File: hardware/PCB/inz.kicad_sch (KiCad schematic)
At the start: 15 parts, among them J101 TP4056, J102 Battery, J103 STM32blackpill

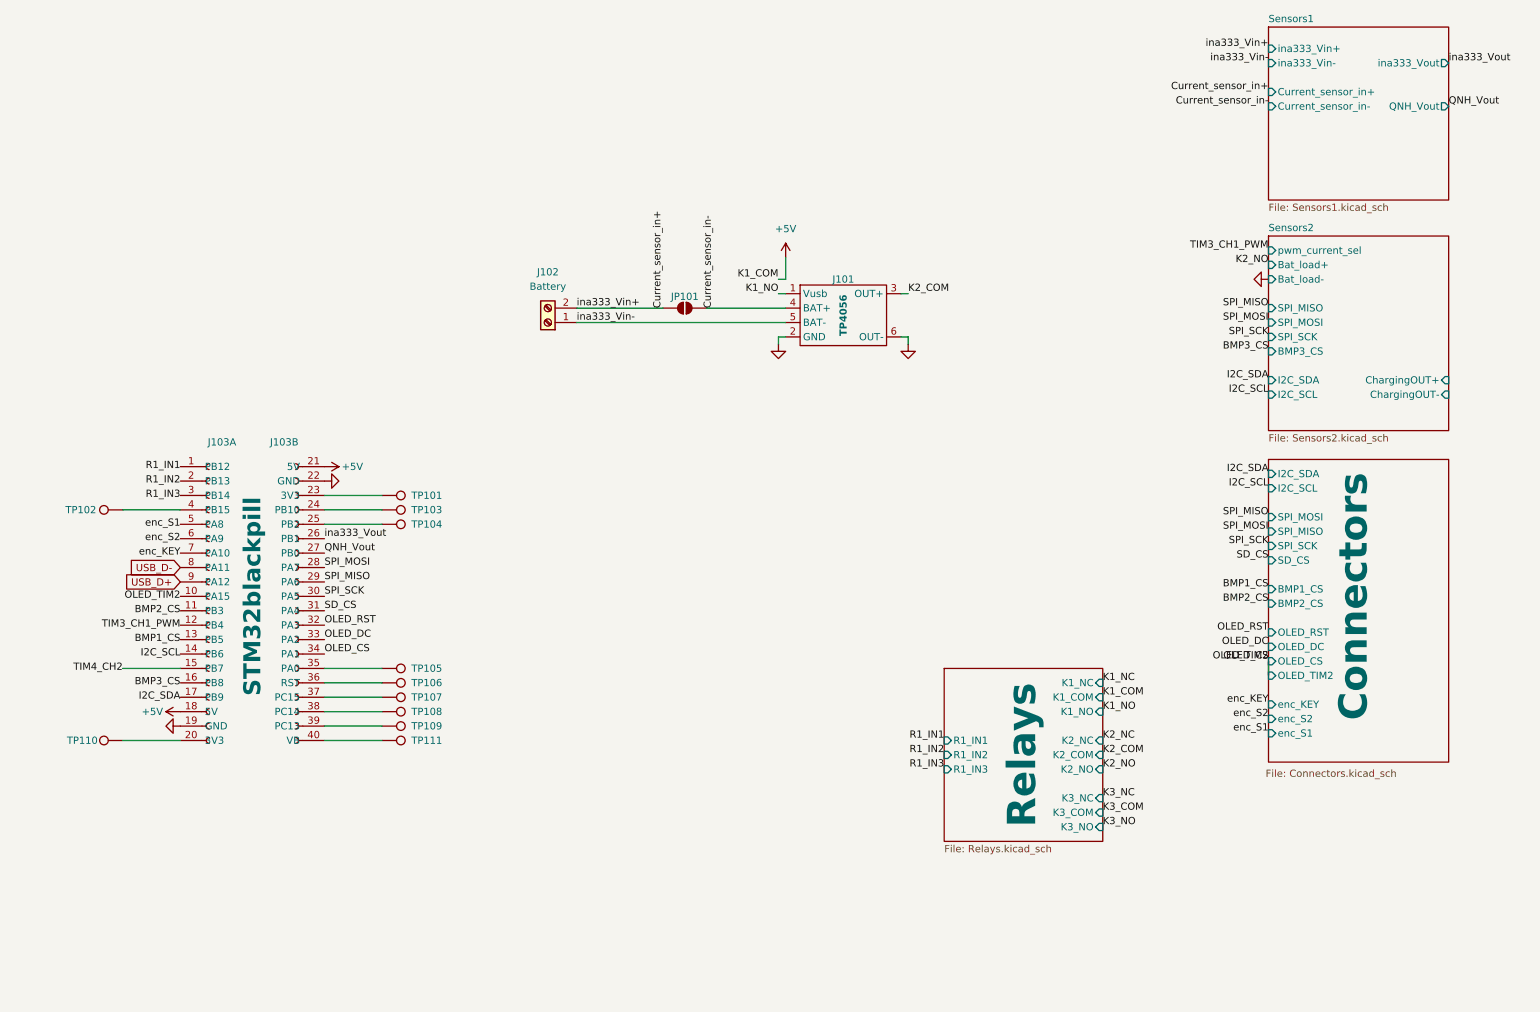
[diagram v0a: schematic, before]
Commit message: XL4015 CC, relays
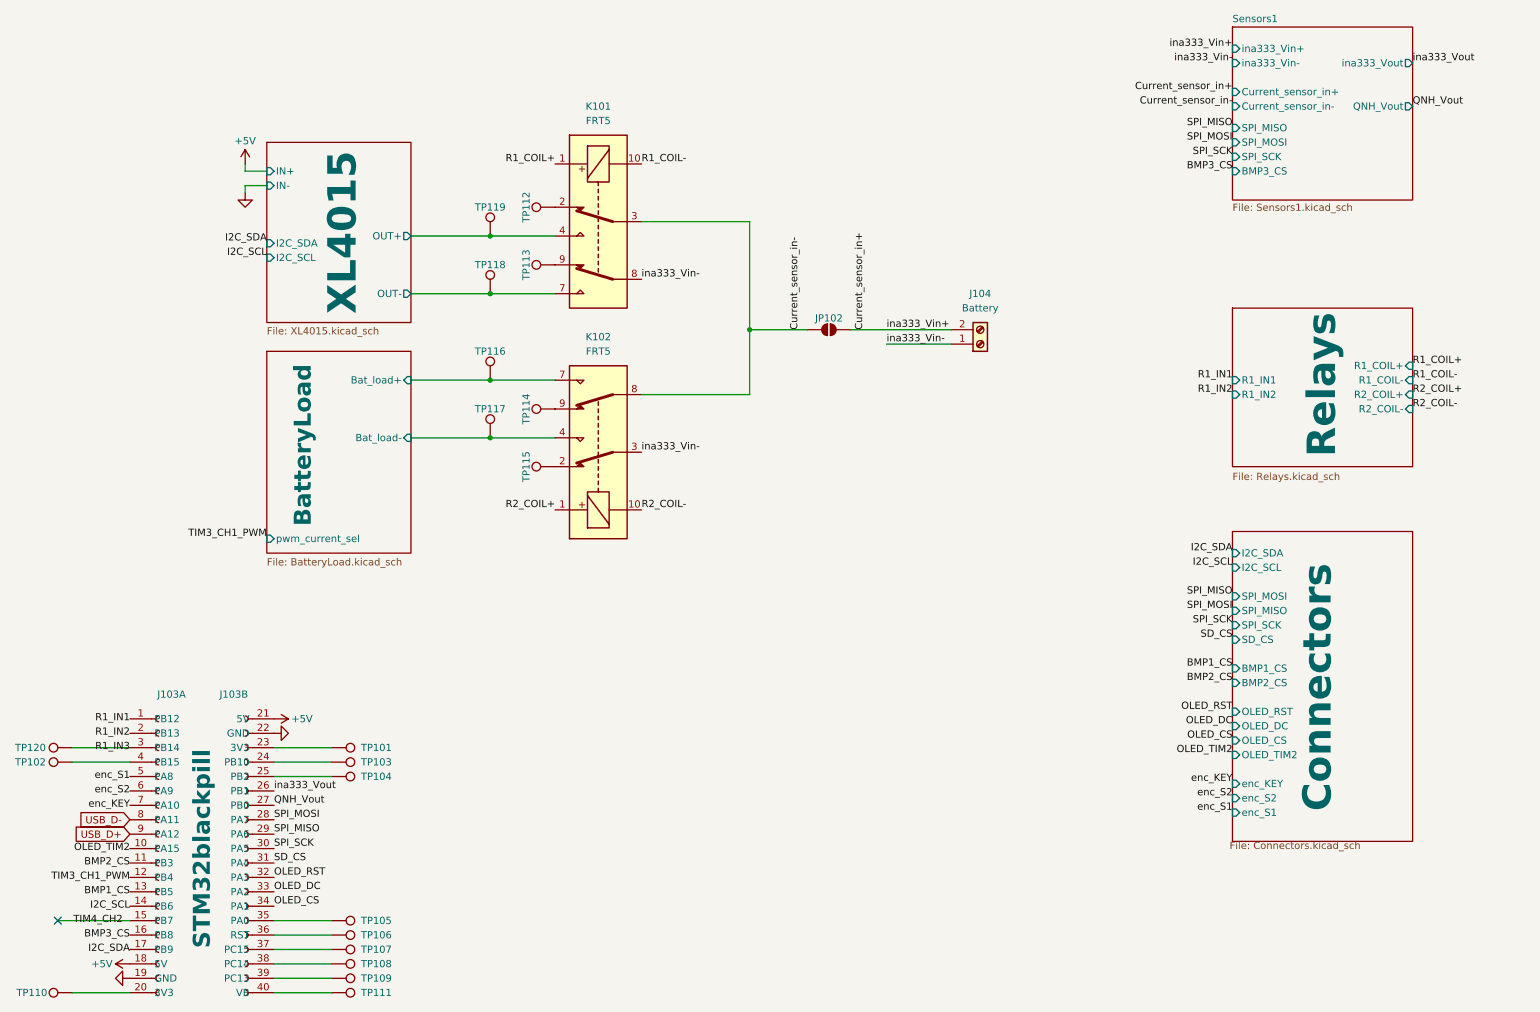
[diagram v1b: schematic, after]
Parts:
- removed J101: TP4056, footprints:board_TP4056, symbol footprints:TP4056
- removed J102: Battery, TerminalBlock_Phoenix:TerminalBlock_Phoenix_MKDS-1,5-2_1x02_P5.00mm_Horizontal, symbol Connector:Screw_Terminal_01x02
- removed JP101: SolderJumper_2_Open, Jumper:SolderJumper-2_P1.3mm_Open_TrianglePad1.0x1.5mm, symbol Jumper:SolderJumper_2_Open
- added J104: Battery, TerminalBlock_Phoenix:TerminalBlock_Phoenix_MKDS-1,5-2_1x02_P5.00mm_Horizontal, symbol Connector:Screw_Terminal_01x02
- added JP102: SolderJumper_2_Open, Jumper:SolderJumper-2_P1.3mm_Open_TrianglePad1.0x1.5mm, symbol Jumper:SolderJumper_2_Open
- added K101, K102: FRT5, Relay_THT:Relay_DPDT_FRT5, symbol Relay:FRT5
- added TP112, TP113, TP114, TP115, TP116, TP117, TP118, TP119, TP120: TestPoint, TestPoint:TestPoint_Pad_D1.5mm, symbol Connector:TestPoint
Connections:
- net Current_sensor_in+: now also J104.2 (Pin_2), JP102.1 (A)
- net Current_sensor_in-: now also JP102.2 (B), K101.3, K102.8
- net OLED_CS: no longer J103.10 (PA15)
- net R1_IN3: now also TP120.1
- net ina333_Vin-: now also J104.1 (Pin_1), K101.8, K102.3
- new net: K102.9, TP114.1
- new net: K101.2, TP112.1
- new net: K101.9, TP113.1
- new net: K102.2, TP115.1
- new net BatteryLoad/Bat_load+: K102.7, TP116.1
- new net BatteryLoad/Bat_load-: K102.4, TP117.1
- new net OLED_TIM2: J103.10 (PA15)
- new net R1_COIL+: K101.1
- new net R1_COIL-: K101.10
- new net R2_COIL+: K102.1
- new net R2_COIL-: K102.10
- new net XL4015/OUT+: K101.4, TP119.1
- new net XL4015/OUT-: K101.7, TP118.1
- no-connect marks 0 -> 1
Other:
- removed sheet Sensors2
- added sheet BatteryLoad (BatteryLoad.kicad_sch)
- added sheet XL4015 (XL4015.kicad_sch)
- sheet Relays ports: added R1_COIL+, R1_COIL-, R2_COIL+, R2_COIL-; removed K1_COM, K1_NC, K1_NO, K2_COM, K2_NC, K2_NO, K3_COM, K3_NC, K3_NO, R1_IN3
- sheet Sensors1 ports: added BMP3_CS, SPI_MISO, SPI_MOSI, SPI_SCK; removed none
- moved on the sheet: J103A, J103B, TP101, TP102, TP103, TP104, TP105, TP106, TP107, TP108, TP109, TP110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

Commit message: pcb
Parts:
- removed TP116, TP117, TP118, TP119: TestPoint, TestPoint:TestPoint_Pad_D1.5mm, symbol Connector:TestPoint
- added JP102: Jumper_2_Bridged, Connector_PinHeader_2.54mm:PinHeader_1x02_P2.54mm_Vertical, symbol Jumper:SolderJumper_2_Bridged
- added TP110: TestPoint, TestPoint:TestPoint_THTPad_D1.5mm_Drill0.7mm, symbol Connector:TestPoint
- TP101: renamed from TP112; footprint TestPoint:TestPoint_Pad_D1.5mm -> TestPoint:TestPoint_THTPad_D1.5mm_Drill0.7mm
- TP102: renamed from TP113; footprint TestPoint:TestPoint_Pad_D1.5mm -> TestPoint:TestPoint_THTPad_D1.5mm_Drill0.7mm
- TP103: renamed from TP114; footprint TestPoint:TestPoint_Pad_D1.5mm -> TestPoint:TestPoint_THTPad_D1.5mm_Drill0.7mm
- TP104: renamed from TP115; footprint TestPoint:TestPoint_Pad_D1.5mm -> TestPoint:TestPoint_THTPad_D1.5mm_Drill0.7mm
- TP105: renamed from TP120; footprint TestPoint:TestPoint_Pad_D1.5mm -> TestPoint:TestPoint_THTPad_D1.5mm_Drill0.7mm
- TP106: renamed from TP101; footprint TestPoint:TestPoint_Pad_D1.5mm -> TestPoint:TestPoint_THTPad_D1.5mm_Drill0.7mm
- TP107: renamed from TP102; footprint TestPoint:TestPoint_Pad_D1.5mm -> TestPoint:TestPoint_THTPad_D1.5mm_Drill0.7mm
- TP108: renamed from TP103; footprint TestPoint:TestPoint_Pad_D1.5mm -> TestPoint:TestPoint_THTPad_D1.5mm_Drill0.7mm
- TP109: renamed from TP104; footprint TestPoint:TestPoint_Pad_D1.5mm -> TestPoint:TestPoint_THTPad_D1.5mm_Drill0.7mm
- TP111: renamed from TP105; footprint TestPoint:TestPoint_Pad_D1.5mm -> TestPoint:TestPoint_THTPad_D1.5mm_Drill0.7mm
- TP112: renamed from TP106; footprint TestPoint:TestPoint_Pad_D1.5mm -> TestPoint:TestPoint_THTPad_D1.5mm_Drill0.7mm
- TP113: renamed from TP107; footprint TestPoint:TestPoint_Pad_D1.5mm -> TestPoint:TestPoint_THTPad_D1.5mm_Drill0.7mm
- TP114: renamed from TP108; footprint TestPoint:TestPoint_Pad_D1.5mm -> TestPoint:TestPoint_THTPad_D1.5mm_Drill0.7mm
- TP115: renamed from TP109; footprint TestPoint:TestPoint_Pad_D1.5mm -> TestPoint:TestPoint_THTPad_D1.5mm_Drill0.7mm
- TP116: renamed from TP110; footprint TestPoint:TestPoint_Pad_D1.5mm -> TestPoint:TestPoint_THTPad_D1.5mm_Drill0.7mm
- TP117: renamed from TP111; footprint TestPoint:TestPoint_Pad_D1.5mm -> TestPoint:TestPoint_THTPad_D1.5mm_Drill0.7mm
- renumbered J104 to J101, J103 to J102, JP102 to JP101
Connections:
- net TIM4_CH2: now also TP110.1
- net ina333_Vin-: now also JP102.1 (A); no longer J101.1 (Pin_1)
- net Current_sensor_in+ renamed BAT_Vin+
- new net: K101.5, K101.6
- new net: K102.5, K102.6
- new net BAT_Vin-: J101.1 (Pin_1), JP102.2 (B)
- no-connect marks 1 -> 2
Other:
- moved on the sheet: JP101

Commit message: PCB routing
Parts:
- removed K101, K102: FRT5, Relay_THT:Relay_DPDT_FRT5, symbol Relay:FRT5
- added RL101, RL102: JW2, Relay_THT:Relay_DPDT_Panasonic_JW2, symbol Relay:JW2
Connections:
- net BatteryLoad/Bat_load+: now also RL102.5
- net BatteryLoad/Bat_load-: now also RL102.4
- net Current_sensor_in-: now also RL101.3, RL102.6
- net R1_COIL+: now also RL101.1
- net R1_COIL-: now also RL101.8
- net R2_COIL+: now also RL102.1
- net R2_COIL-: now also RL102.8
- net XL4015/OUT+: now also RL101.4
- net XL4015/OUT-: now also RL101.5
- net ina333_Vin-: now also RL101.6, RL102.3
- net at TP103.1: now also RL102.7
- net at TP101.1: now also RL101.2
- net at TP102.1: now also RL101.7
- net at TP104.1: now also RL102.2
- no-connect marks 2 -> 0

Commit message: PCB final routing
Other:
- company: (none) -> Authors: D. Ledzianowski K. Lewandowska T. Majchrzak
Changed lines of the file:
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@@
 	(generator_version "9.0")
 	(paper "A4")
+	(title_block
+		(date "2025-12-07")
+		(rev "1.0")
+		(company "Authors: D. Ledzianowski K. Lewandowska T. Majchrzak")
+	)
 	(junction
 		(at 142.24 69.85)

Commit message: PCB final design
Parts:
- J101, JP102, RL101, RL102: now not fitted
- J102: footprint footprints:STM32blackpill -> Package_DIP:DIP-40_W15.24mm; JLCPCB Part (none) -> C2332; Link https://pl.aliexpress.com/item/1005001456186625.html?spm=a2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 -> https://jlcpcb.com/partdetail/2706-ICSockets40P/C2332; MFR Part (none) -> ICSockets-40P; Manufacturer (none) -> BOOMELE(Boom Precision Elec)
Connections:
- net +5V: now also J102.40 (5V); no longer J102.21 (5V)
- net GND: now also J102.39 (GND); no longer J102.22 (GND)
- net OLED_CS: now also J102.27 (PA1); no longer J102.34 (PA1)
- net OLED_DC: now also J102.28 (PA2); no longer J102.33 (PA2)
- net OLED_RST: now also J102.29 (PA3); no longer J102.32 (PA3)
- net QNH_Vout: now also J102.34 (PB0); no longer J102.27 (PB0)
- net SD_CS: now also J102.30 (PA4); no longer J102.31 (PA4)
- net SPI_MISO: now also J102.32 (PA6); no longer J102.29 (PA6)
- net SPI_MOSI: now also J102.33 (PA7); no longer J102.28 (PA7)
- net SPI_SCK: now also J102.31 (PA5); no longer J102.30 (PA5)
- net ina333_Vout: now also J102.35 (PB1); no longer J102.26 (PB1)
- net at TP108.1: now also J102.37 (PB10); no longer J102.24 (PB10)
- net at TP109.1: now also J102.36 (PB2); no longer J102.25 (PB2)
- net at J102.23 (PC14): now also TP114.1; no longer TP106.1
- net at TP111.1: now also J102.26 (PA0); no longer J102.35 (PA0)
- net at TP112.1: now also J102.25 (RST); no longer J102.36 (RST)
- net at TP113.1: now also J102.24 (PC15); no longer J102.37 (PC15)
- net at J102.38 (3V3): now also TP106.1; no longer TP114.1
- net at TP115.1: now also J102.22 (PC13); no longer J102.39 (PC13)
- net at TP117.1: now also J102.21 (VB); no longer J102.40 (VB)
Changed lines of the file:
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@@
 		(in_bom no)
 		(on_board yes)
-		(dnp no)
+		(dnp yes)
 		(fields_autoplaced yes)
 		(property "Reference" "J101"
@@
 		(in_bom no)
 		(on_board yes)
-		(dnp no)
+		(dnp yes)
 		(property "Reference" "JP102"
 			(at 165.1 74.676 0)
@@
 			)
 		)
-		(property "Footprint" "footprints:STM32blackpill"
+		(property "Footprint" "Package_DIP:DIP-40_W15.24mm"
 			(at 62.23 161.29 0)
 			(effects
@@
 			)
 		)
-		(property "Datasheet" ""
+		(property "Datasheet" "https://pl.aliexpress.com/item/1005001456186625.html?spm=a2g0o.order_list.order_list_main.5.5b641c24b7gB50&gatewayAdapt=glo2pol"
 			(at 62.23 161.29 0)
 			(effects
@@
 			)
 		)
-		(property "Link" "https://pl.aliexpress.com/item/1005001456186625.html?spm=a2g0o.order_list.order_list_main.5.5b641c24b7gB50&gatewayAdapt=glo2pol"
+		(property "Link" "https://jlcpcb.com/partdetail/2706-ICSockets40P/C2332"
 			(at 62.23 161.29 0)
 			(effects
@@
 		)
 		(property "Sim.Type" ""
+			(at 62.23 161.29 0)
+			(effects
+				(font
+					(size 1.27 1.27)
+				)
+				(hide yes)
+			)
+		)
+		(property "JLCPCB Part" "C2332"
+			(at 62.23 161.29 0)
+			(effects
+				(font
+					(size 1.27 1.27)
+				)
+				(hide yes)
+			)
+		)
+		(property "MFR Part" "ICSockets-40P"
+			(at 62.23 161.29 0)
+			(effects
+				(font
+					(size 1.27 1.27)
+				)
+				(hide yes)
+			)
+		)
+		(property "Manufacturer" "BOOMELE(Boom Precision Elec)"
 			(at 62.23 161.29 0)
 			(effects
@@
 		(in_bom no)
 		(on_board yes)
-		(dnp no)
+		(dnp yes)
 		(property "Reference" "RL102"
 			(at 121.92 71.12 90)
@@
 		(in_bom no)
 		(on_board yes)
-		(dnp no)
+		(dnp yes)
 		(fields_autoplaced yes)
 		(property "Reference" "RL101"
@@
 			)
 		)
-		(property "Footprint" "footprints:STM32blackpill"
+		(property "Footprint" "Package_DIP:DIP-40_W15.24mm"
 			(at 41.91 161.29 0)
 			(effects
@@
 			)
 		)
-		(property "Datasheet" ""
+		(property "Datasheet" "https://pl.aliexpress.com/item/1005001456186625.html?spm=a2g0o.order_list.order_list_main.5.5b641c24b7gB50&gatewayAdapt=glo2pol"
 			(at 41.91 161.29 0)
 			(effects
@@
 			)
 		)
-		(property "Link" "https://pl.aliexpress.com/item/1005001456186625.html?spm=a2g0o.order_list.order_list_main.5.5b641c24b7gB50&gatewayAdapt=glo2pol"
+		(property "Link" "https://jlcpcb.com/partdetail/2706-ICSockets40P/C2332"
 			(at 41.91 161.29 0)
 			(effects
@@
 			)
 		)
+		(property "JLCPCB Part" "C2332"
+			(at 41.91 161.29 0)
+			(effects
+				(font
+					(size 1.27 1.27)
+				)
+				(hide yes)
+			)
+		)
+		(property "MFR Part" "ICSockets-40P"
+			(at 41.91 161.29 0)
+			(effects
+				(font
+					(size 1.27 1.27)
+				)
+				(hide yes)
+			)
+		)
+		(property "Manufacturer" "BOOMELE(Boom Precision Elec)"
+			(at 41.91 161.29 0)
+			(effects
+				(font
+					(size 1.27 1.27)
+				)
+				(hide yes)
+			)
+		)
 		(pin "18"
 		)
@@
 		(pin "2"
 		)
+		(pin "20"
+		)
+		(pin "22"
+		)
+		(pin "23"
+		)
+		(pin "32"
+		)
+		(pin "25"
+		)
 		(pin "24"
 		)
-		(pin "22"
-		)
-		(pin "23"
-		)
-		(pin "32"
-		)
-		(pin "25"
-		)
-		(pin "20"
-		)
 		(pin "3"

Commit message: oled, sd
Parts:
- J102: footprint Package_DIP:DIP-40_W15.24mm -> footprints:STM32blackpill
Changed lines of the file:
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@@
 			)
 		)
-		(property "Footprint" "Package_DIP:DIP-40_W15.24mm"
+		(property "Footprint" "footprints:STM32blackpill"
 			(at 62.23 161.29 0)
 			(effects
@@
 			)
 		)
-		(property "Footprint" "Package_DIP:DIP-40_W15.24mm"
+		(property "Footprint" "footprints:STM32blackpill"
 			(at 41.91 161.29 0)
 			(effects

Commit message: usb, sd
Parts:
- J101, JP102, RL101, RL102: now fitted
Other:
- title: (none) -> Stanowisko do badania parametrów pracy ogniw Li-Ion Li-Pol
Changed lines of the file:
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@@
 	(paper "A4")
 	(title_block
-		(date "2025-12-07")
-		(rev "1.0")
+		(title "Stanowisko do badania parametrów pracy ogniw Li-Ion Li-Pol")
+		(date "2025-12-10")
+		(rev "0.1")
 		(company "Authors: D. Ledzianowski K. Lewandowska T. Majchrzak")
 	)
@@
 		(in_bom no)
 		(on_board yes)
-		(dnp yes)
+		(dnp no)
 		(fields_autoplaced yes)
 		(property "Reference" "J101"
@@
 		(in_bom no)
 		(on_board yes)
-		(dnp yes)
+		(dnp no)
 		(property "Reference" "JP102"
 			(at 165.1 74.676 0)
@@
 		(in_bom no)
 		(on_board yes)
-		(dnp yes)
+		(dnp no)
 		(property "Reference" "RL102"
 			(at 121.92 71.12 90)
@@
 		(in_bom no)
 		(on_board yes)
-		(dnp yes)
+		(dnp no)
 		(fields_autoplaced yes)
 		(property "Reference" "RL101"
